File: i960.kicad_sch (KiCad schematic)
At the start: 50 parts

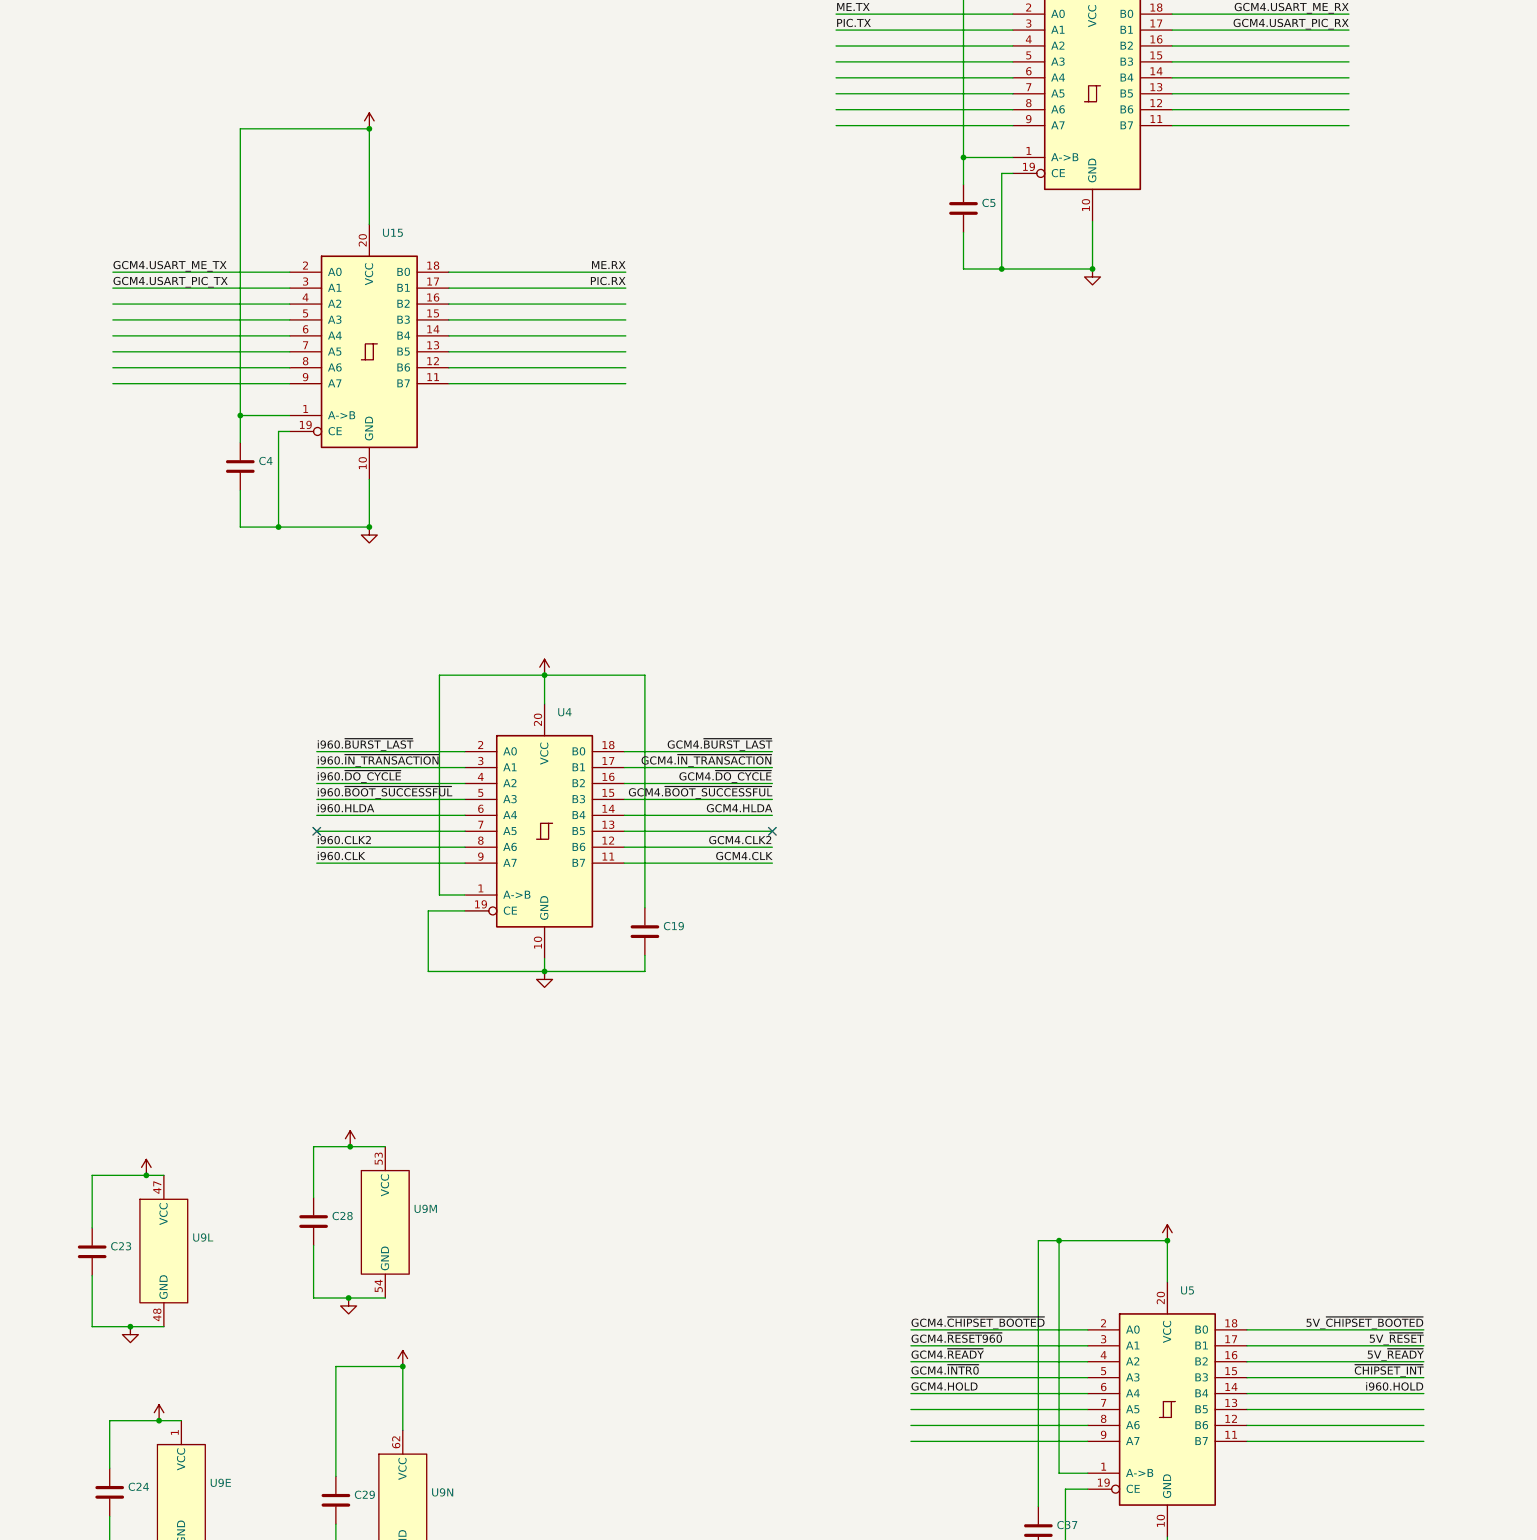
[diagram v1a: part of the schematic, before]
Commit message: Save an AHC245 by reducing the number of interrupts accessible by the chipset
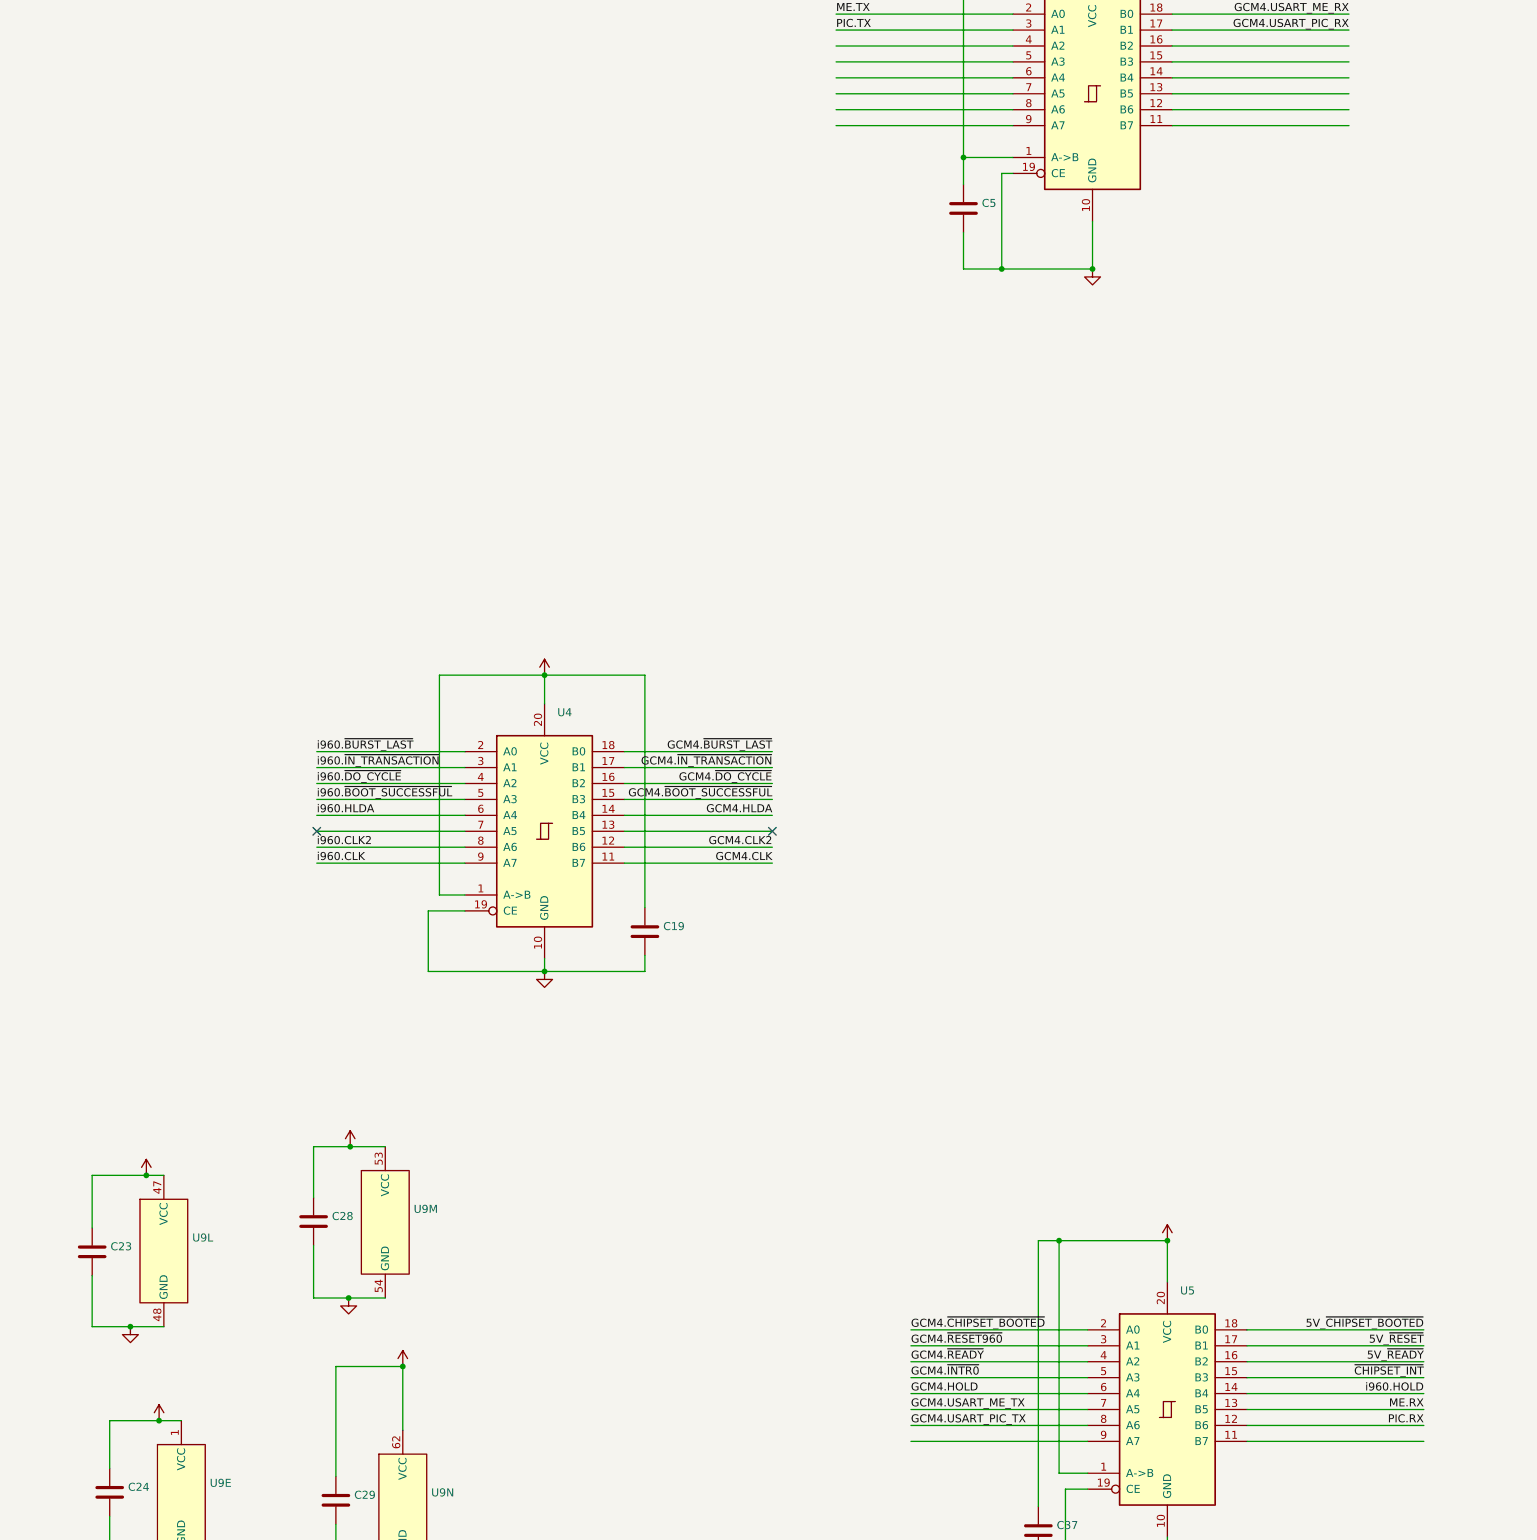
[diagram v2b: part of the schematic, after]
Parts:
- removed C4: (no value), symbol Device:C
- removed U15: (no value), symbol 74xx:74HC245
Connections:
- net GCM4.USART_ME_TX: now also U5.7 (A5)
- net GCM4.USART_PIC_TX: now also U5.8 (A6)
- net ME.RX: now also U5.13 (B5)
- net PIC.RX: now also U5.12 (B6)

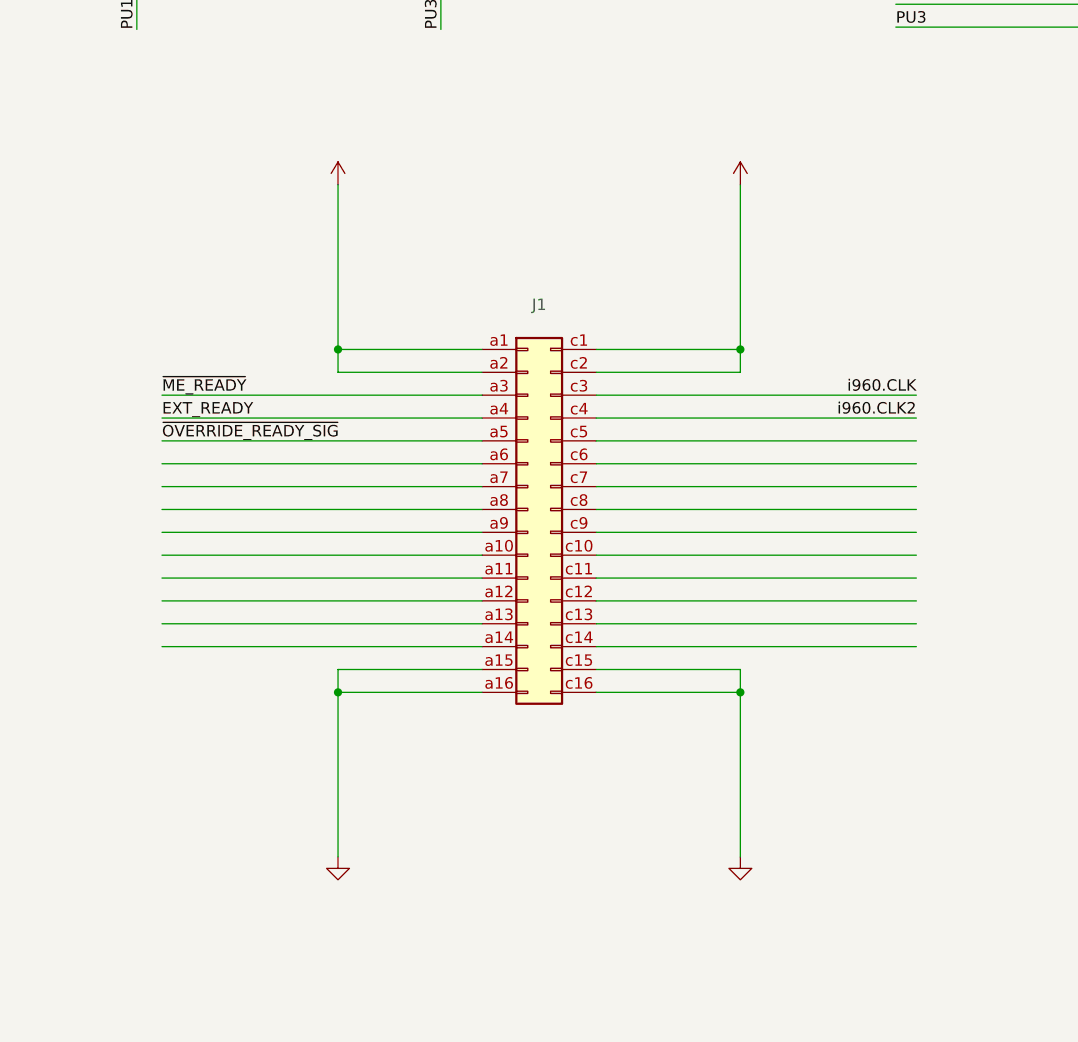
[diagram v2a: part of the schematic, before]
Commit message: Drop the external connector for overriding.
I think I'm just going to add the two synchronizers as a backup but put
the edge detection logic into the CCL as the backup
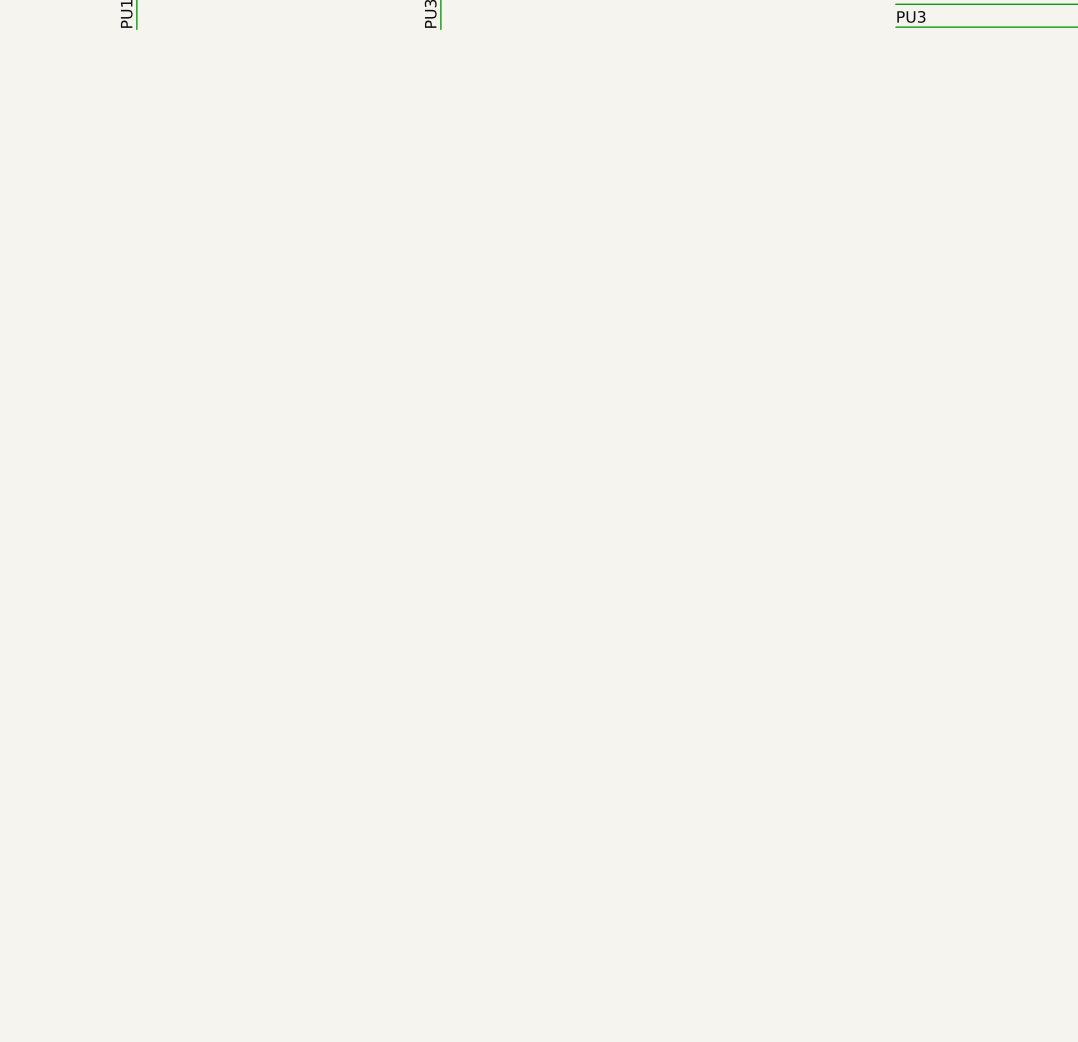
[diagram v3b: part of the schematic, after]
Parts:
- removed J1: (no value), symbol Connector:DIN41612_02x16_AC

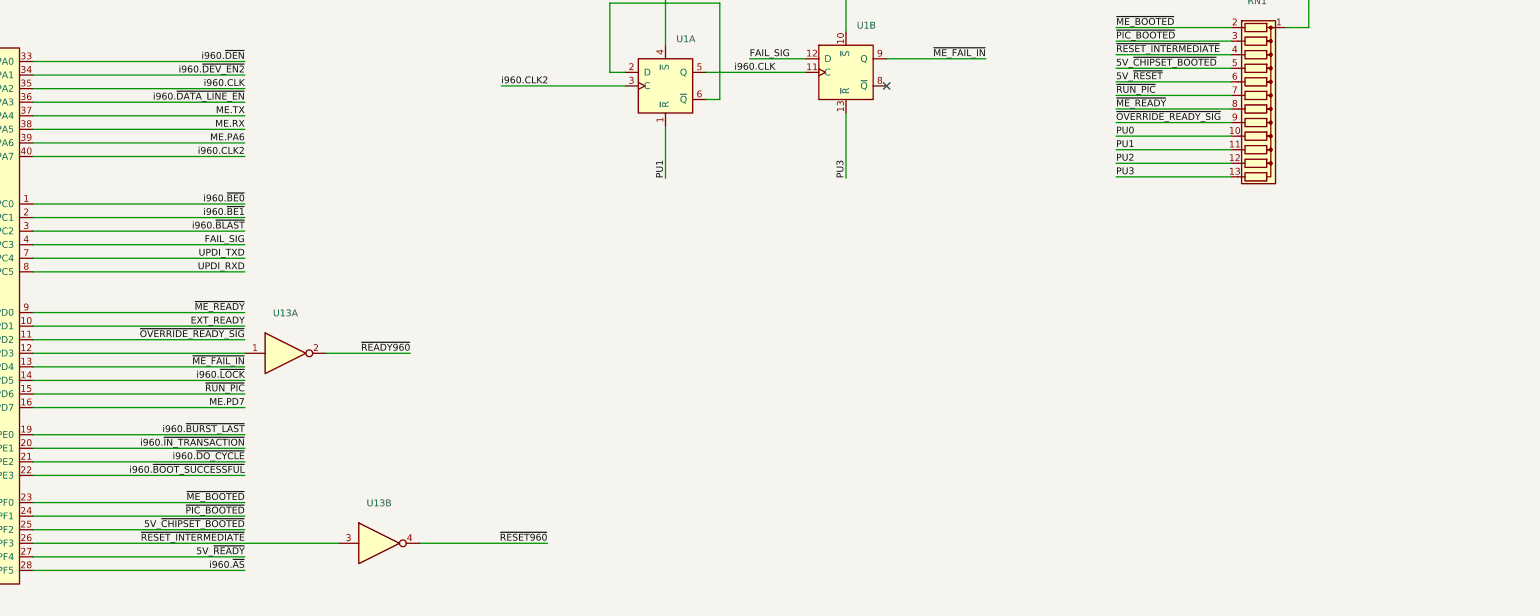
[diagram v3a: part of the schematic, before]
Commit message: Put the falling edge detector flip-flops on the main board.
It will be connected to IN1 and IN2 of CCL2. I am going to add a jumper
block to allow this extra flip flop block to be activated
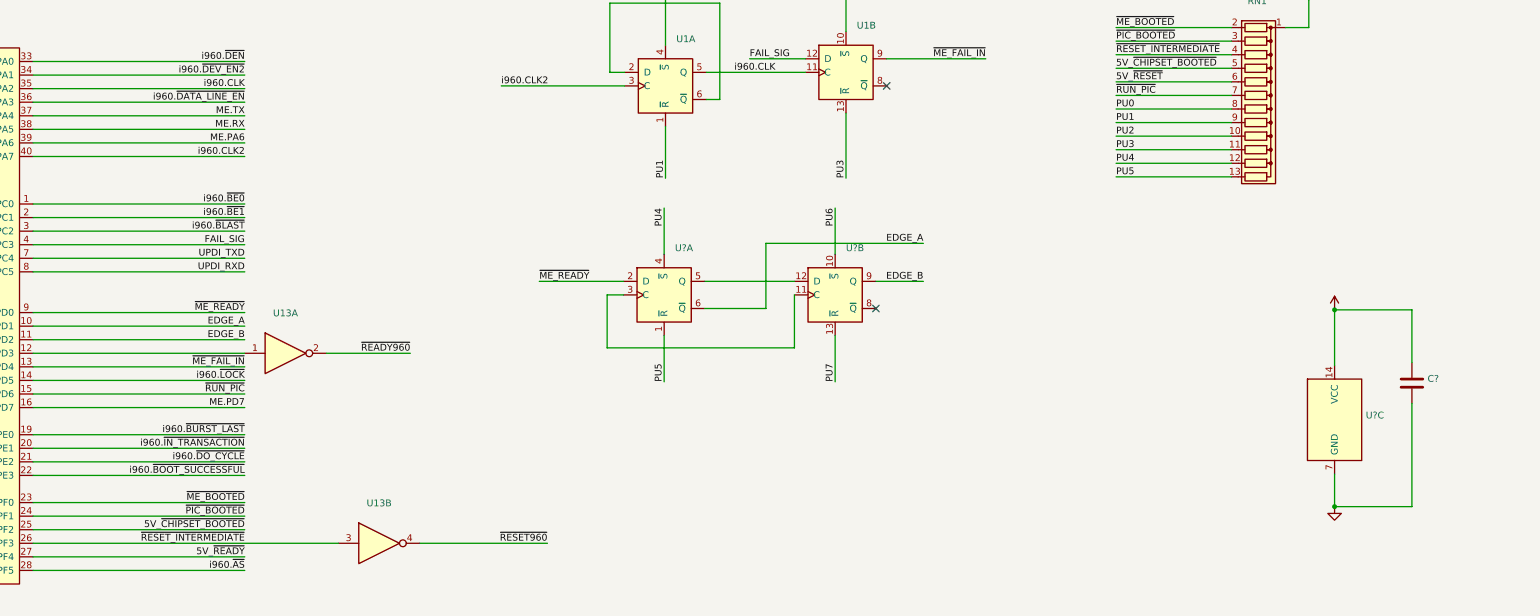
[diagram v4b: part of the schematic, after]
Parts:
- added C?: (no value), symbol Device:C
- added U? (x3): (no value), symbol 74xx:74HC74
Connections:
- net +5V: now also C?.1, U?.14 (VCC)
- net GND: now also C?.2, U?.7 (GND)
- net PU0: now also RN1.8 (R7); no longer RN1.10 (R9)
- net PU1: now also RN1.9 (R8); no longer RN1.11 (R10)
- net PU2: now also RN1.10 (R9); no longer RN1.12 (R11)
- net PU3: now also RN1.11 (R10); no longer RN1.13 (R12)
- net ~{ME_READY}: now also U?.2 (D); no longer RN1.8 (R7)
- net EXT_READY renamed EDGE_A
- net EDGE_A: now also U?.6 (~{Q})
- net ~{OVERRIDE_READY_SIG} renamed EDGE_B
- net EDGE_B: now also U?.9 (Q); no longer RN1.9 (R8)
- new net: U?.11 (C), U?.3 (C)
- new net: U?.12 (D), U?.5 (Q)
- new net PU4: RN1.12 (R11), U?.4 (~{S})
- new net PU5: RN1.13 (R12), U?.1 (~{R})
- new net PU6: U?.10 (~{S})
- new net PU7: U?.13 (~{R})
- no-connect marks 5 -> 6
